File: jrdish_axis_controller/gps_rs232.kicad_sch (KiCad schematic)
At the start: 19 parts, among them CN10 KF2EDGR-2.54-2P, CN11 KF2EDGR-2.54-3P, Q3 2N7002, U8 SP3232EEY-L/TR

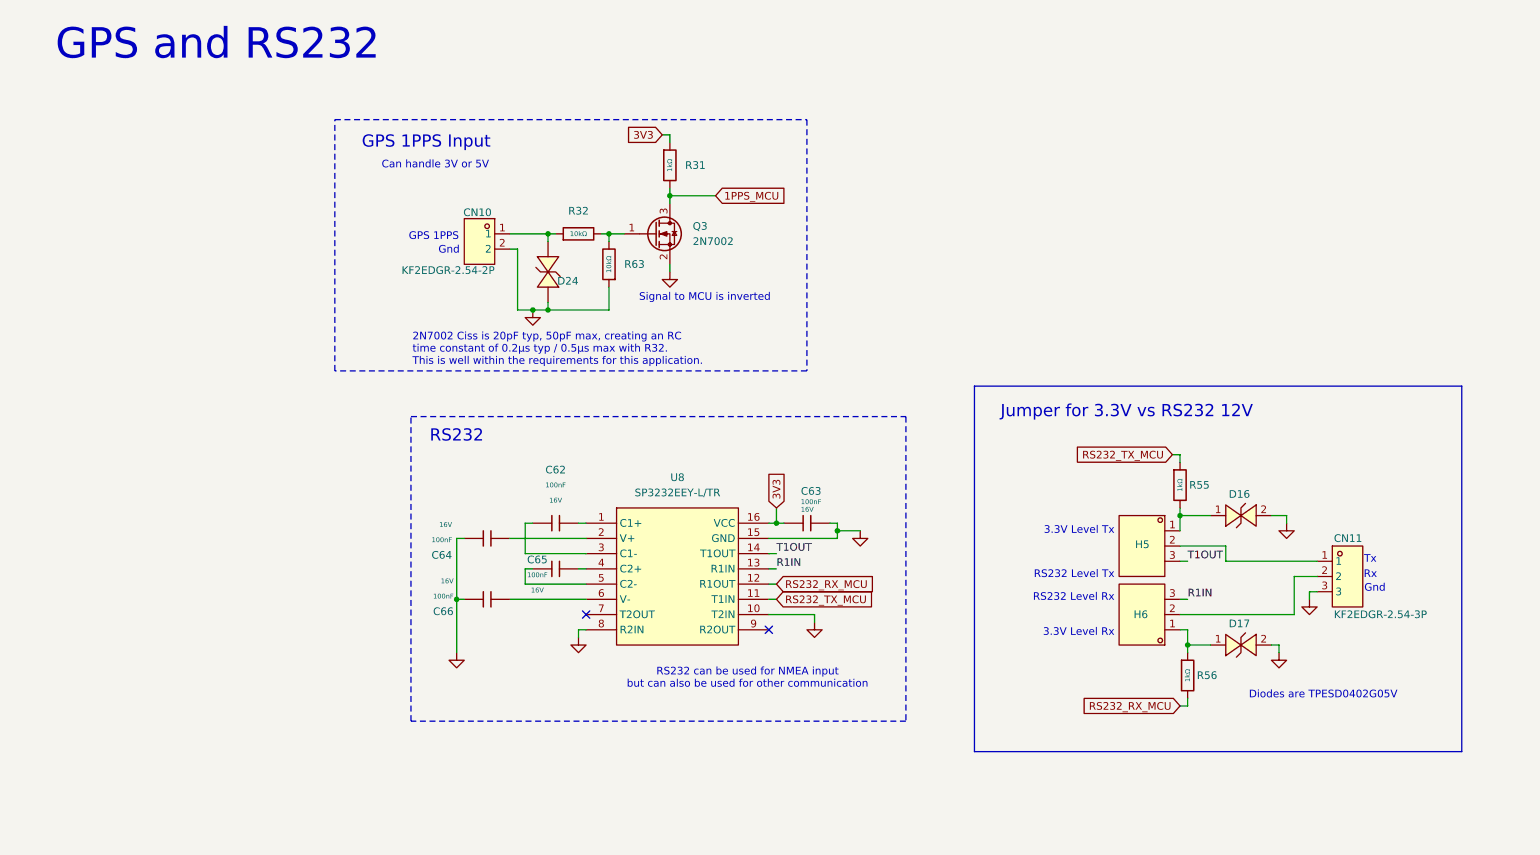
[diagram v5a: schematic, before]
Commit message: Limit switches with mosfets
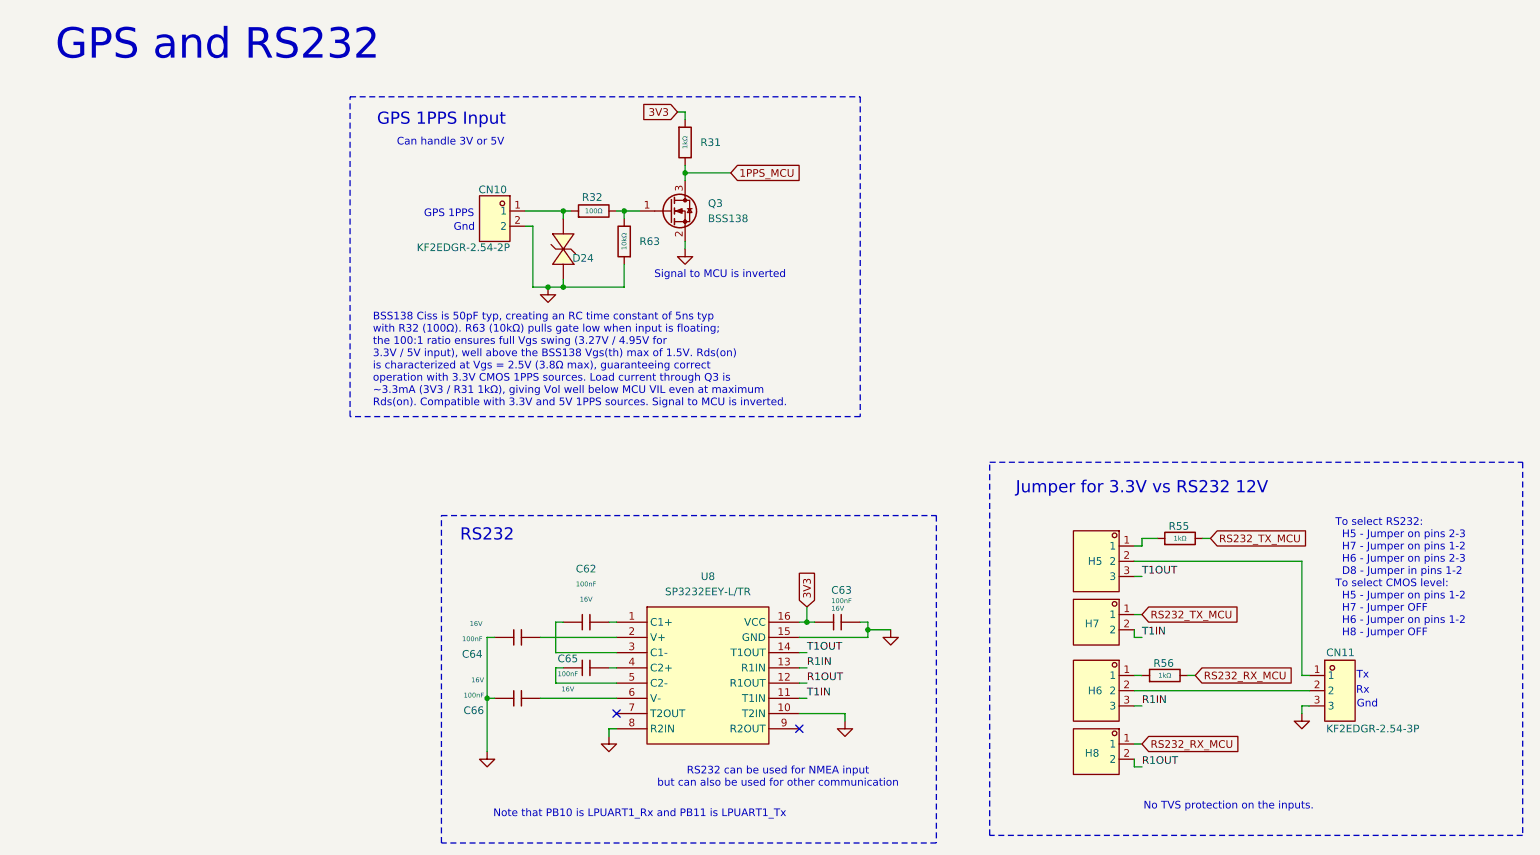
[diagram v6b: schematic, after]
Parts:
- removed D16, D17: TPESD0402G05V, MyParts:D0402-BI, symbol MyParts:TPESD0402G05V
- removed Q3: 2N7002, Package_TO_SOT_SMD:SOT-23, symbol Transistor_FET:2N7002
- removed R32: 10kΩ, PCM_JLCPCB:R_0402, symbol PCM_JLCPCB-Resistors:0402,10kΩ
- added H7, H8: 210S-1*2P L=11.6MMGold-plated black, MyParts:HDR-TH_2P-P2.54-V-M-1, symbol MyParts:210S-1*2PL=11.6MMGold-platedblack
- added Q3: BSS138, Package_TO_SOT_SMD:SOT-23, symbol Transistor_FET:BSS138
- added R32: 100Ω, PCM_JLCPCB:R_0402, symbol PCM_JLCPCB-Resistors:0402,100Ω
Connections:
- net 1PPS_MCU: now also Q3.3 (D)
- net RS232_RX_MCU: now also H8.1; no longer U8.12 (R1OUT)
- net RS232_TX_MCU: now also R55.2, H7.1; no longer R55.1, U8.11 (T1IN)
- net at H5.1: now also R55.1; no longer R55.2
- net at CN10.1, D24.1 (K): now also R32.1
- net GND: now reaches CN10.2, D24.2 (A), R63.1
- net GND: now also C63.2, C64.1, C66.1, CN11.3, U8.10 (T2IN), U8.15 (GND), U8.8 (R2IN), Q3.2 (S)
- net at R63.2: now also Q3.1 (G), R32.2
- new net R1OUT: H8.2, U8.12 (R1OUT)
- new net T1IN: H7.2, U8.11 (T1IN)
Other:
- note added: "BSS138 Ciss is 50pF typ, creating an RC time constant of 5ns typ with R32 (100Ω). R63 (10kΩ) pulls gate low when input is floating; the 100:1 ratio ensures full Vgs swing (3.27V / 4.95V for 3.3V / 5V input), well above the BSS138 Vgs(th) max of 1.5V. Rds(on) is characterized at Vgs = 2.5V (3.8Ω max), guaranteeing correct operation with 3.3V CMOS 1PPS sources. Load current through Q3 is ~3.3mA (3V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"
- note added: "No TVS protection on the inputs."
- note added: "Note that PB10 is LPUART1_Rx and PB11 is LPUART1_Tx"
- note added: "To select RS232: H5 - Jumper on pins 2-3 H7 - Jumper on pins 1-2 H6 - Jumper on pins 2-3 D8 - Jumper in pins 1-2 To select CMOS level: H5 - Jumper on pins 1-2 H7 - Jumper OFF H6 - Jumper on pins 1-2 H8 - Jumper OFF"
- note removed: "2N7002 Ciss is 20pF typ, 50pF max, creating an RC time constant of 0.2µs typ / 0.5µs max with R32. This is well within the requirements for this application."
- note removed: "3.3V Level Rx"
- note removed: "3.3V Level Tx"
- note removed: "Diodes are TPESD0402G05V"
- note removed: "RS232 Level Rx"
- note removed: "RS232 Level Tx"
- moved on the sheet: C62, C63, C64, C65, C66, CN10, D24, R31, R63, U8

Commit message: Removed RS232 chip, not 3.3V UART only
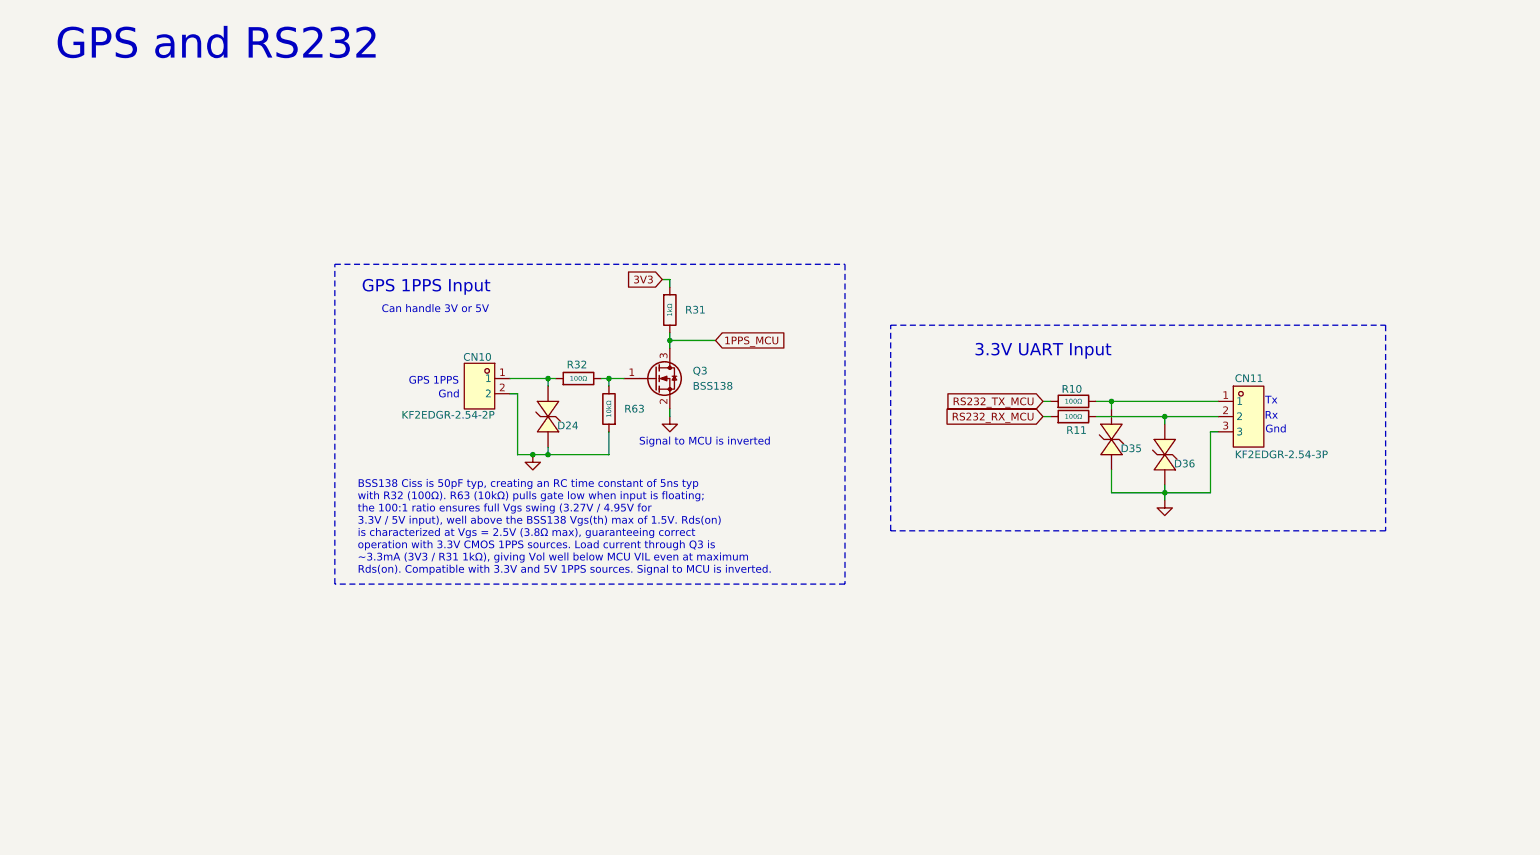
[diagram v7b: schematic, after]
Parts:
- removed C62, C63, C64, C65, C66: 100nF, PCM_JLCPCB:C_0402, symbol PCM_JLCPCB-Capacitors:0402,100nF
- removed H5, H6: 210S-1*3P L=11.6MMGold-plated black, MyParts:HDR-TH_3P-P2.54-V-M-1, symbol MyParts:210S-1*3PL=11.6MMGold-platedblack
- removed H7, H8: 210S-1*2P L=11.6MMGold-plated black, MyParts:HDR-TH_2P-P2.54-V-M-1, symbol MyParts:210S-1*2PL=11.6MMGold-platedblack
- removed R55, R56: 1kΩ, PCM_JLCPCB:R_0402, symbol PCM_JLCPCB-Resistors:0402,1kΩ
- removed U8: SP3232EEY-L/TR, MyParts:TSSOP-16_L5.0-W4.4-P0.65-LS6.4-BL, symbol MyParts:SP3232EEY-L_TR
- added D35, D36: TPESD0402G05V, MyParts:D0402-BI, symbol MyParts:TPESD0402G05V
- added R10, R11: 100Ω, PCM_JLCPCB:R_0402, symbol PCM_JLCPCB-Resistors:0402,100Ω
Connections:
- net GND: now also D35.2 (A), D36.2 (A)
- net RS232_RX_MCU: now also R11.1
- net RS232_TX_MCU: now also R10.1
- net at CN11.2: now also D36.1 (K), R11.2
- net at CN11.1: now also D35.1 (K), R10.2
- no-connect marks 2 -> 0
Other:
- note added: "3.3V UART Input"
- note removed: "Jumper for 3.3V vs RS232 12V"
- note removed: "No TVS protection on the inputs."
- note removed: "Note that PB10 is LPUART1_Rx and PB11 is LPUART1_Tx"
- note removed: "RS232"
- note removed: "RS232 can be used for NMEA input but can also be used for other communication"
- note removed: "To select RS232: H5 - Jumper on pins 2-3 H7 - Jumper on pins 1-2 H6 - Jumper on pins 2-3 D8 - Jumper in pins 1-2 To select CMOS level: H5 - Jumper on pins 1-2 H7 - Jumper OFF H6 - Jumper on pins 1-2 H8 - Jumper OFF"
- moved on the sheet: CN10, D24, Q3, R31, R32, R63
